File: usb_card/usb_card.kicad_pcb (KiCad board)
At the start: 2 copper layers, 27.8 x 31.4 mm, 16 parts, among them J1 DS_Card, J2 USB_OTG, J3 USB_OTG, U1 MAX3421E, Y1 12MHz

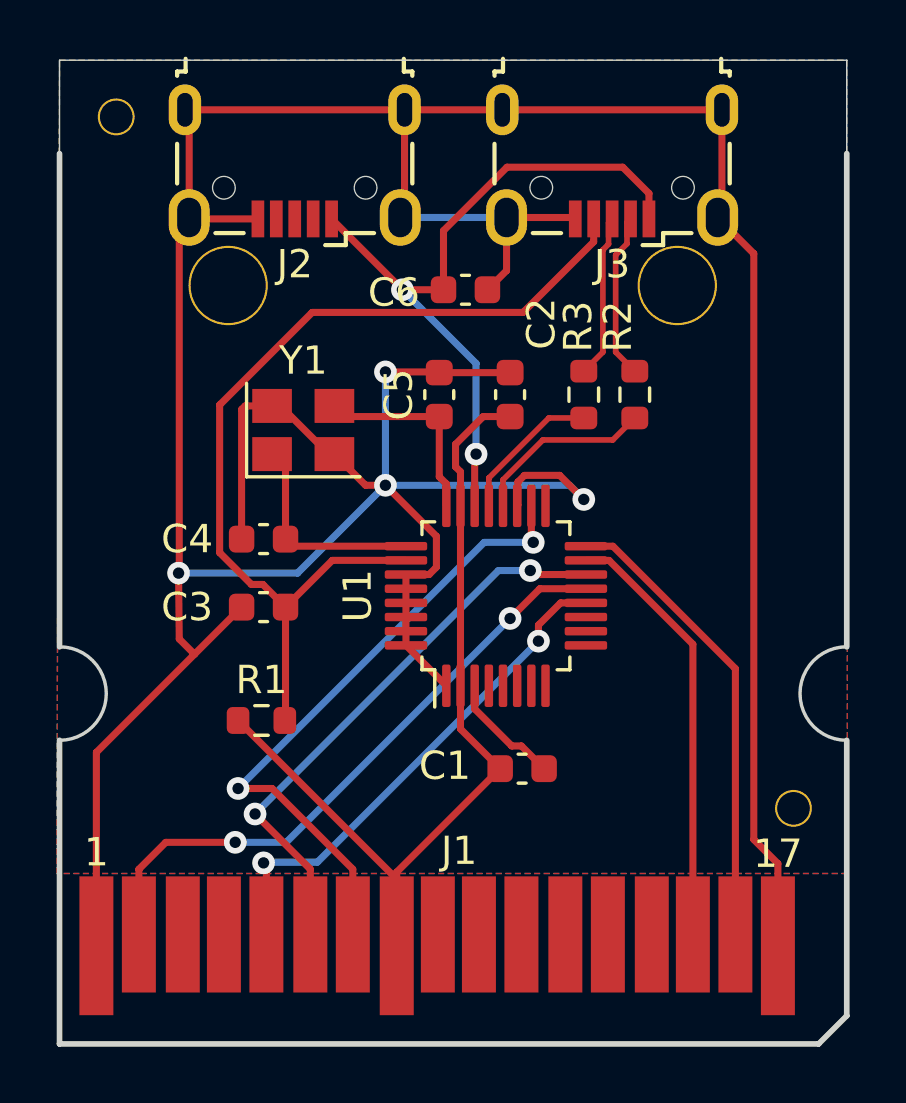
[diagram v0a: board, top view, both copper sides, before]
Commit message: Fix missing GND connection in USB card
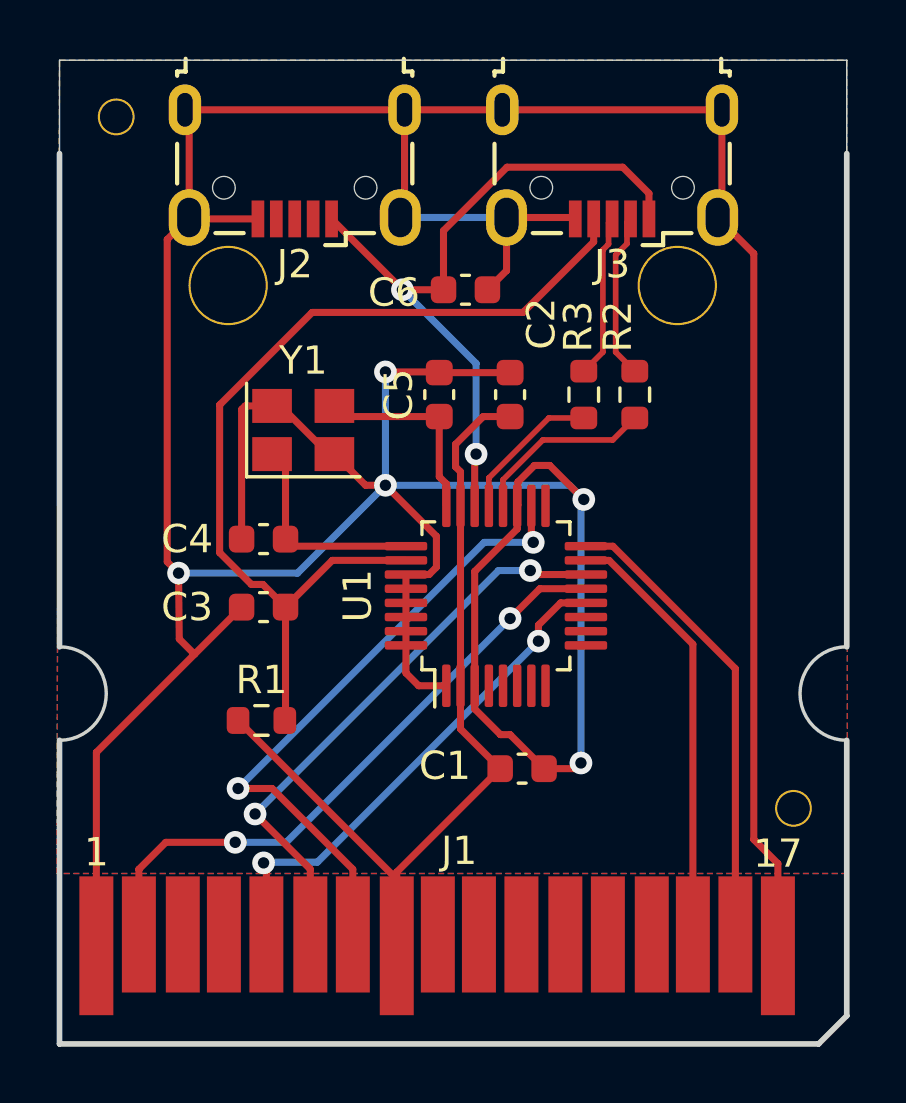
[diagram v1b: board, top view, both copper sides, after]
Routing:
- net GND: track 150.6 -> 169.5 mm, vias 4 -> 5
